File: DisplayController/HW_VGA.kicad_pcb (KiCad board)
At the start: 2 copper layers, 150 x 90 mm, 77 parts, among them J1 Conn_02x40_Odd_Even, J301 Conn_01x02, J401 Conn_01x06, U102 GAL22V10, U103 74ALS163, U104 74ALS163, U105 74ALS163, U202 GAL22V10, U203 74ALS163, U204 74ALS163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

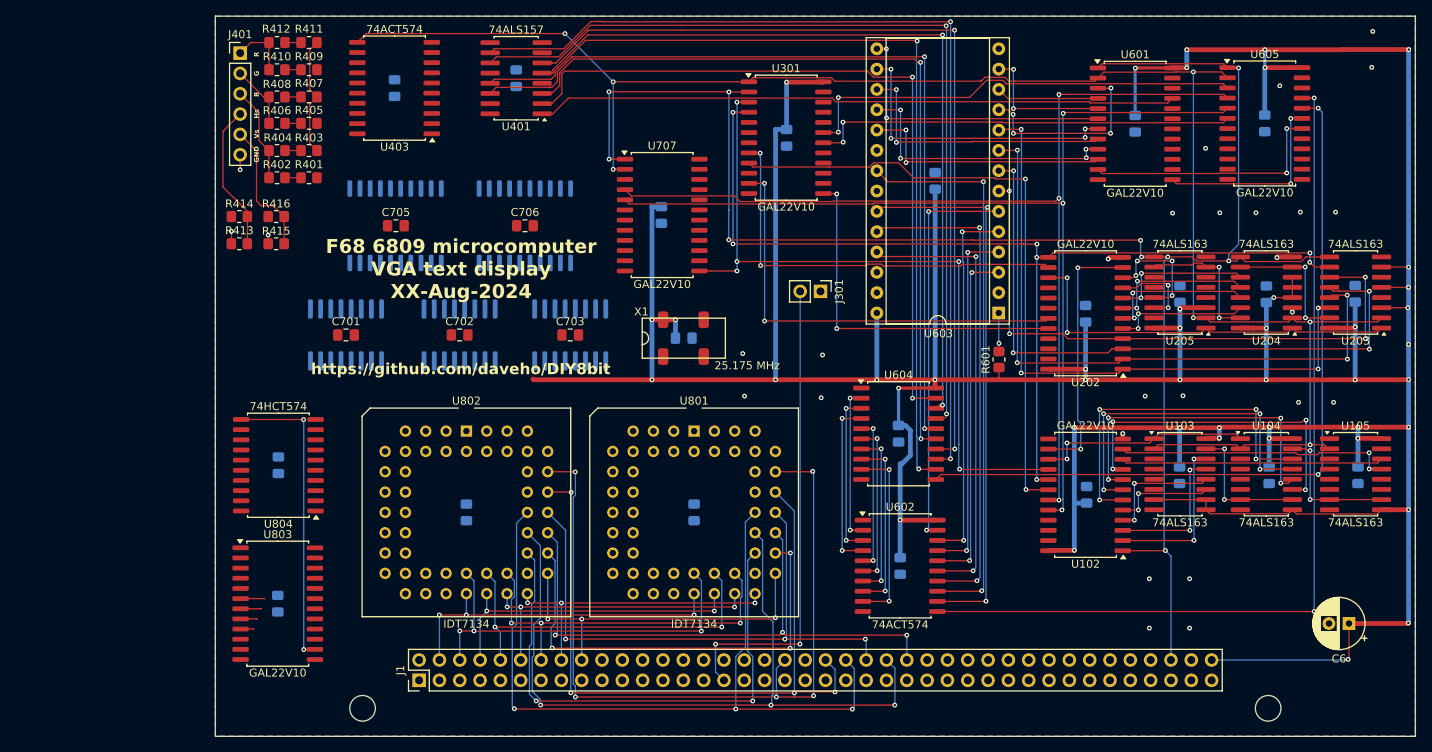
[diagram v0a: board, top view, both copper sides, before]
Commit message: most/all host A/D bus signals are routed
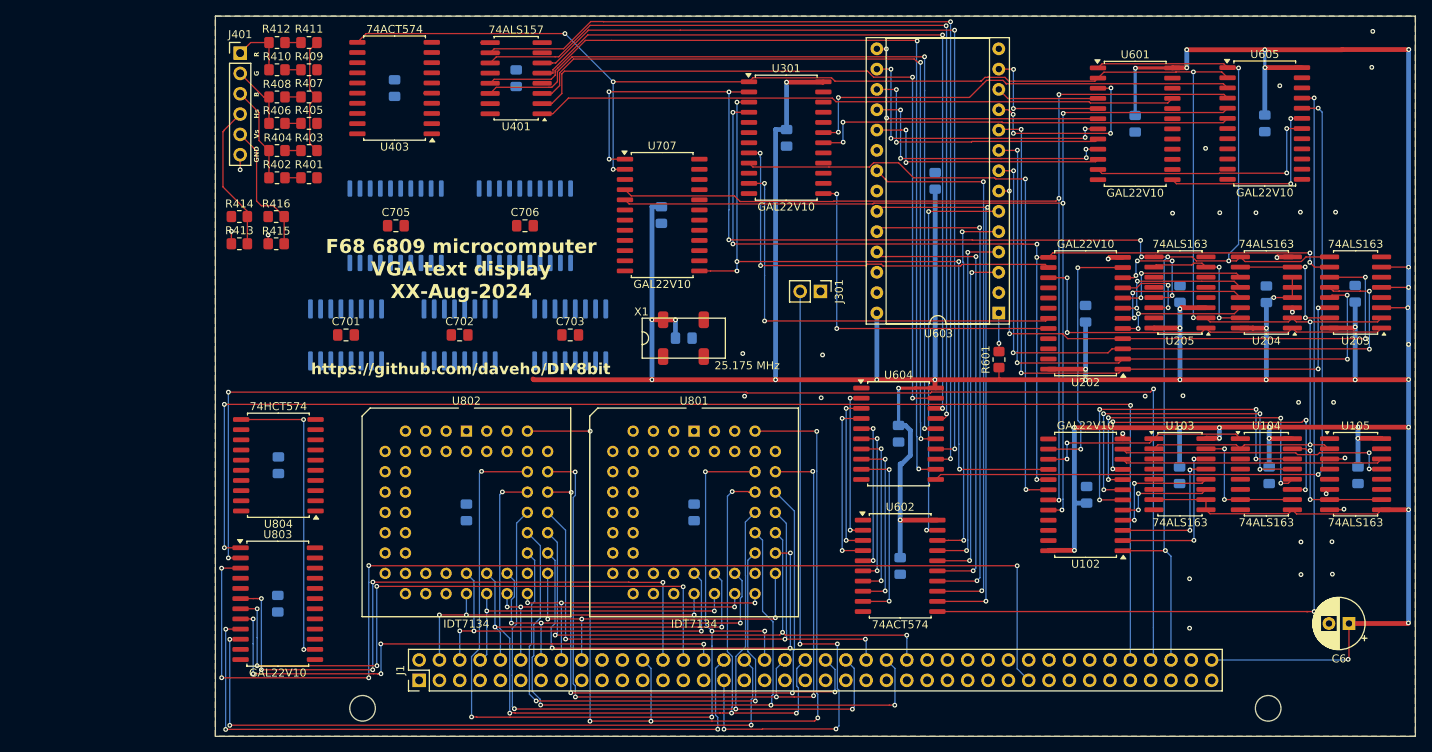
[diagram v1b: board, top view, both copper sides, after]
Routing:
- net /-HostWMEM: track 0.00 -> 172.2 mm, vias 0 -> 3
- net /-HostRMEM: track 0.00 -> 165.1 mm, vias 0 -> 3
- net /~{IODEV7}: track 0.00 -> 144.5 mm, vias 0 -> 5
- net /HostA10: track 0.00 -> 124.5 mm, vias 0 -> 5
- net /HostA0: track 0.00 -> 114.5 mm, vias 0 -> 6
- net /HostA2: track 0.00 -> 105.7 mm, vias 0 -> 5
- net /HostA15: track 0.00 -> 85.9 mm, vias 0 -> 3
- net /HostA14: track 1.65 -> 85.1 mm, vias 0 -> 3
- net /HostA11: track 3.03 -> 82.4 mm, vias 0 -> 5
- net /HostA12: track 2.61 -> 81.6 mm, vias 0 -> 5
- net /HostA13: track 2.08 -> 70.7 mm, vias 0 -> 5
- net /IRQ6: track 59.6 -> 79.8 mm, vias 2 -> 4
- net GND: track 6.96 -> 11.5 mm, vias 26 -> 31

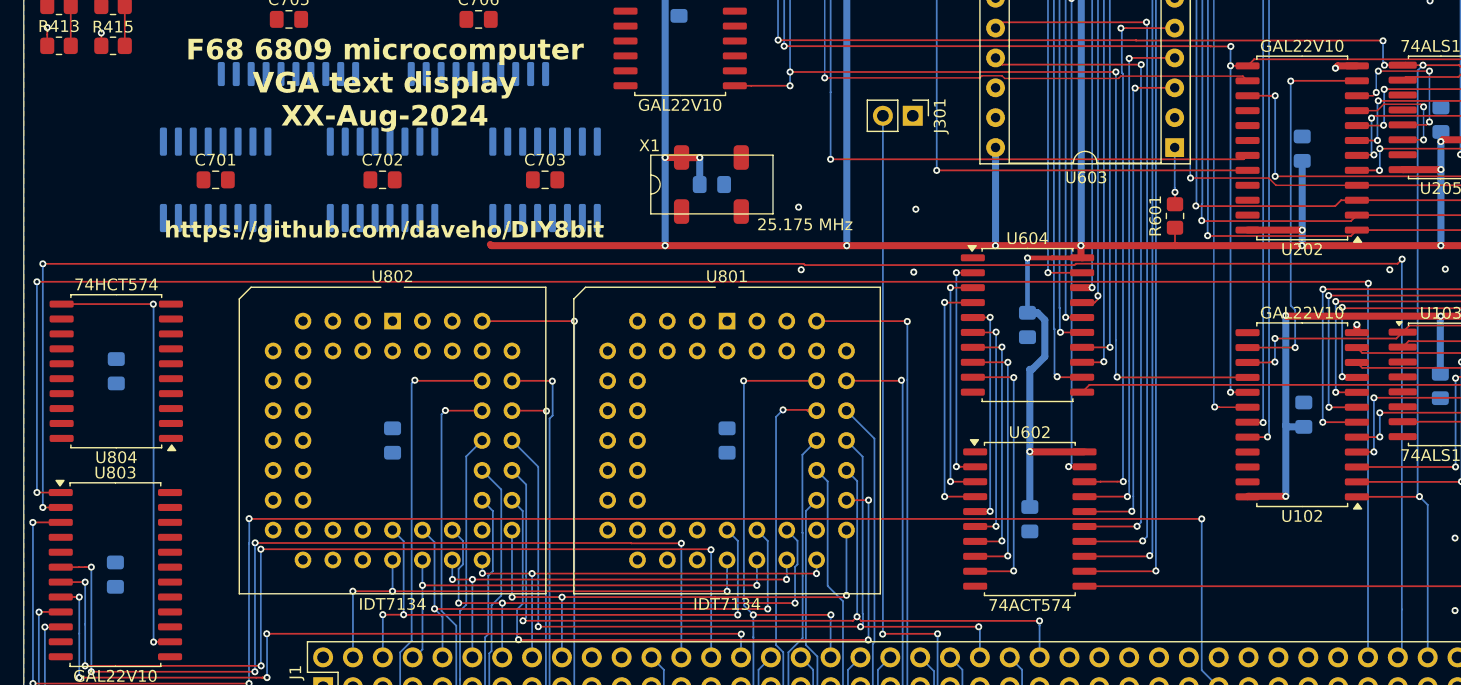
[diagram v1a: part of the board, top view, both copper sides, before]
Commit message: routed some VCC connections
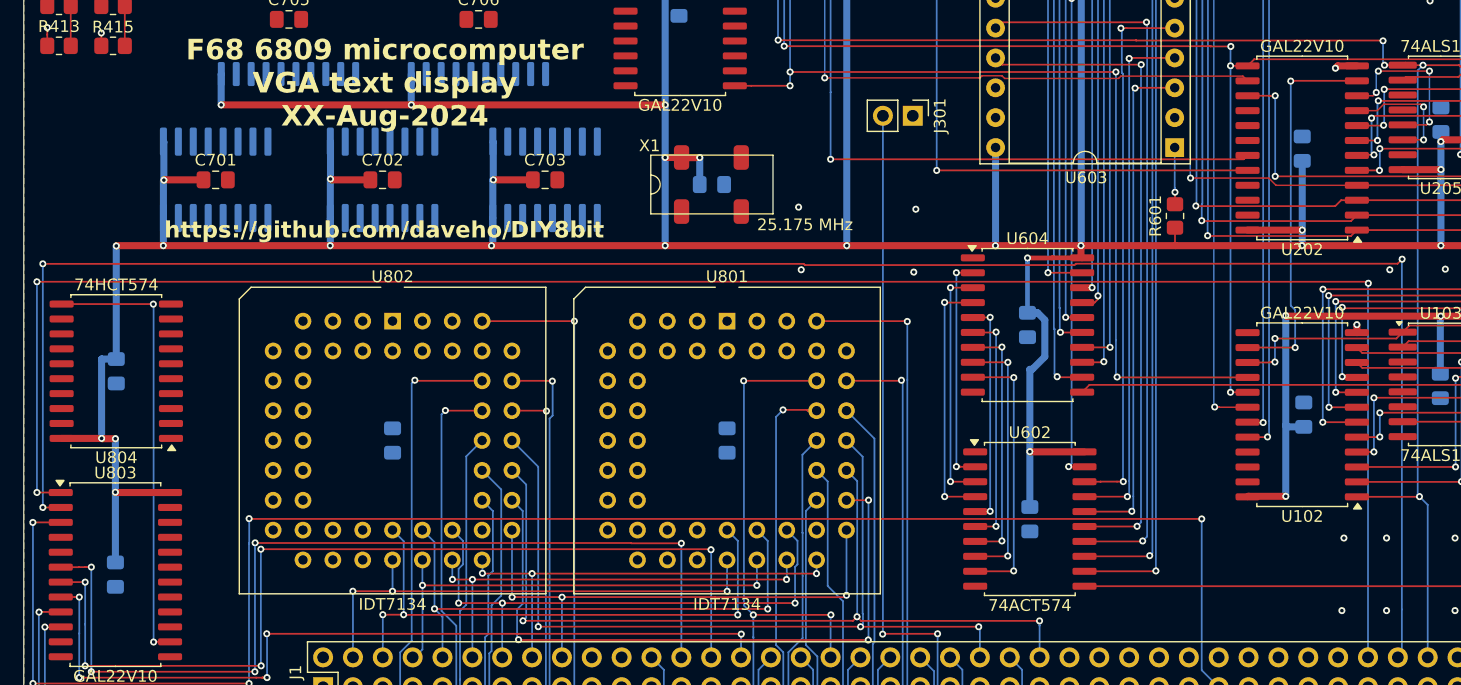
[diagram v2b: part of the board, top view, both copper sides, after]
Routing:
- net VCC: track 593.9 -> 743.0 mm, vias 43 -> 56
- net GND: vias 31 -> 35

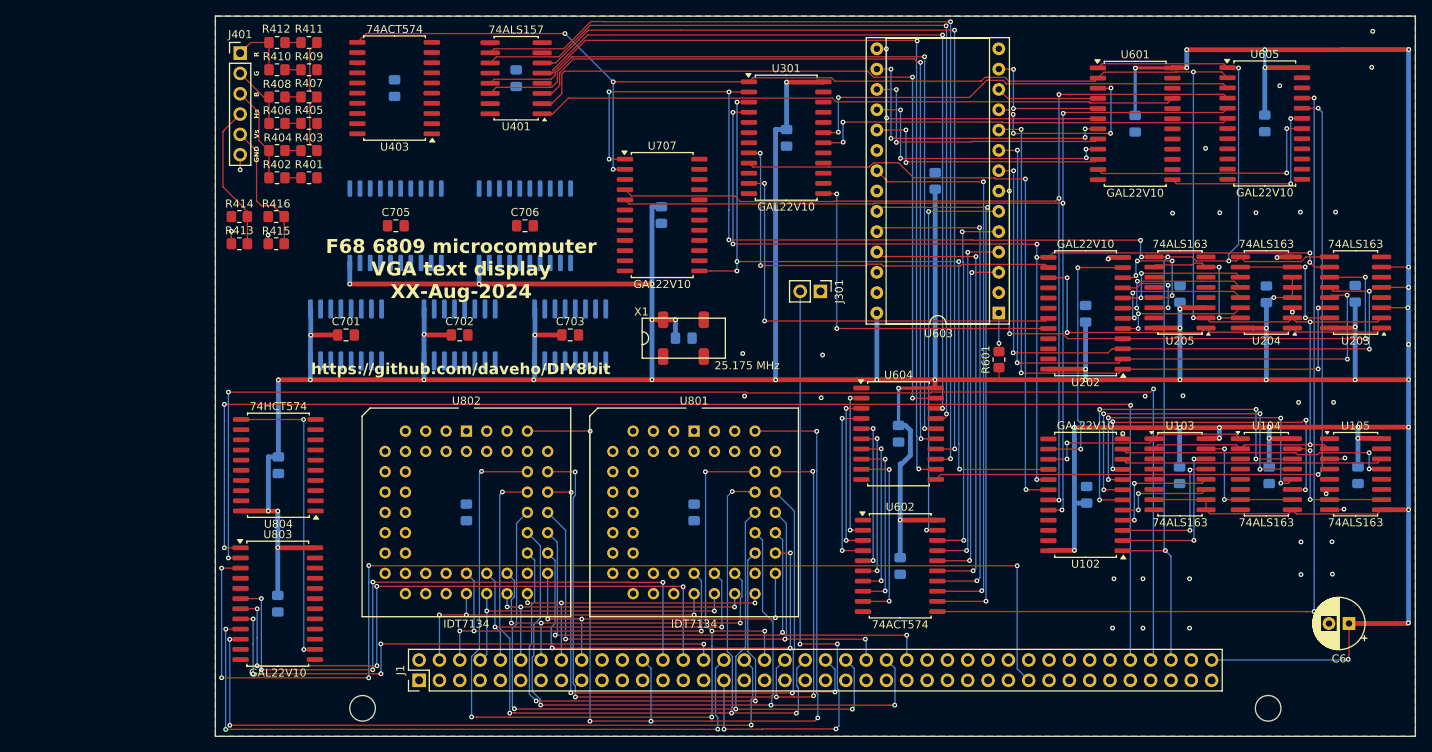
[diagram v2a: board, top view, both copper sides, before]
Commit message: getting close...mostly just the VRAM now
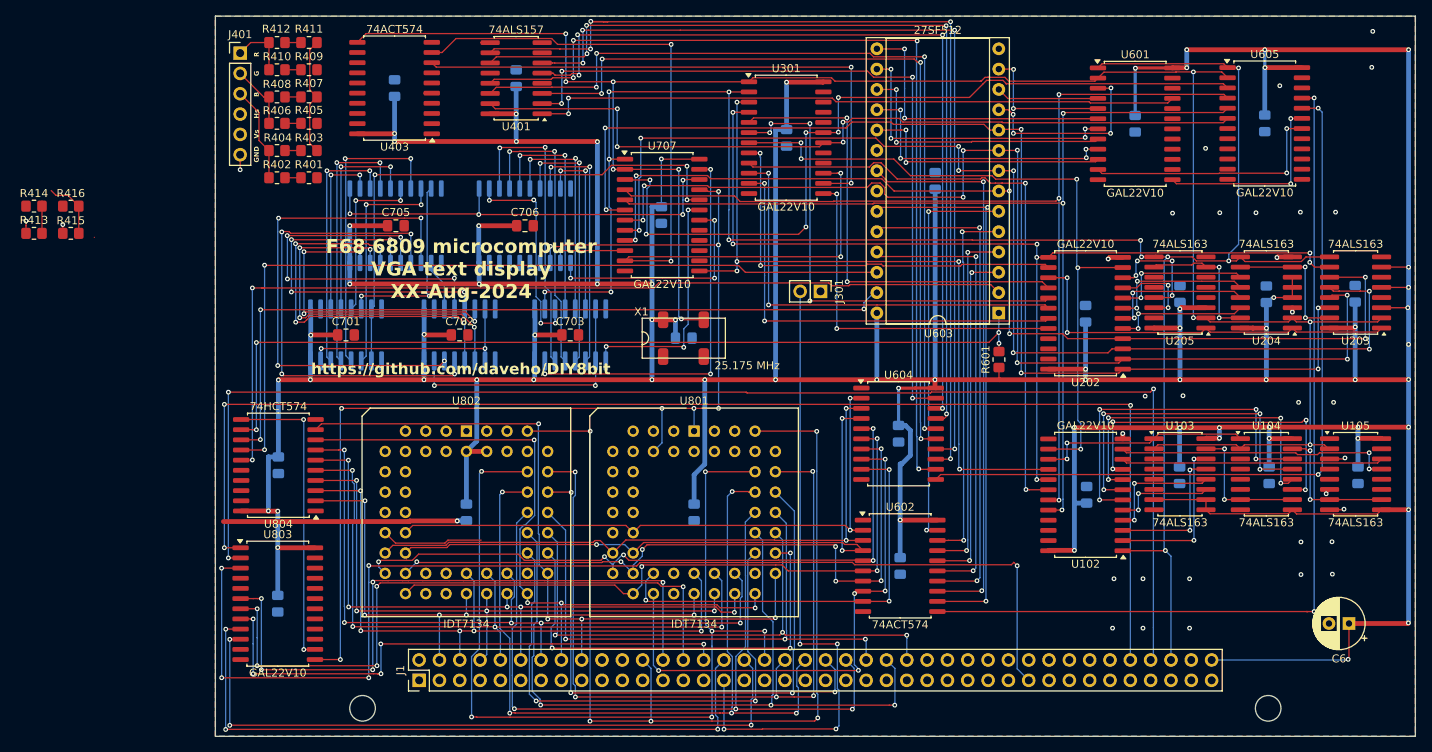
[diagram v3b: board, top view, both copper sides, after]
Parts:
- moved R414 25.7 mm to (40.8, 82.1)
- moved R413 25.7 mm to (40.8, 85.5)
- moved R416 25.7 mm to (45.4, 82.1)
- moved R415 25.7 mm to (45.4, 85.5)
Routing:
- net /ReadoutA12: track 0.00 -> 143.2 mm, vias 0 -> 8
- net VCC: track 743.0 -> 870.8 mm, vias 56 -> 67
- net /FontA12: track 0.00 -> 117.3 mm, vias 0 -> 2
- net /FontA15: track 4.84 -> 111.0 mm, vias 1 -> 4
- net /VSync: track 0.00 -> 103.6 mm, vias 0 -> 4
- net /FontA13: track 0.00 -> 102.9 mm, vias 0 -> 2
- net /FontA14: track 0.00 -> 97.0 mm, vias 0 -> 3
- net /HSync: track 0.00 -> 70.7 mm, vias 0 -> 2
- net /Readout/IncrReadoutAddr: track 0.00 -> 68.7 mm, vias 0 -> 3
- net /ReadoutD3: track 19.3 -> 85.9 mm, vias 2 -> 5
- net /ReadoutD5: track 21.3 -> 86.7 mm, vias 2 -> 7
- net /ReadoutA4: track 0.00 -> 63.0 mm, vias 0 -> 4
- net /VC0: track 79.7 -> 142.3 mm, vias 4 -> 6
- net /VC2: track 81.8 -> 143.5 mm, vias 4 -> 8
- net /ReadoutD4: track 20.3 -> 81.5 mm, vias 2 -> 3
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
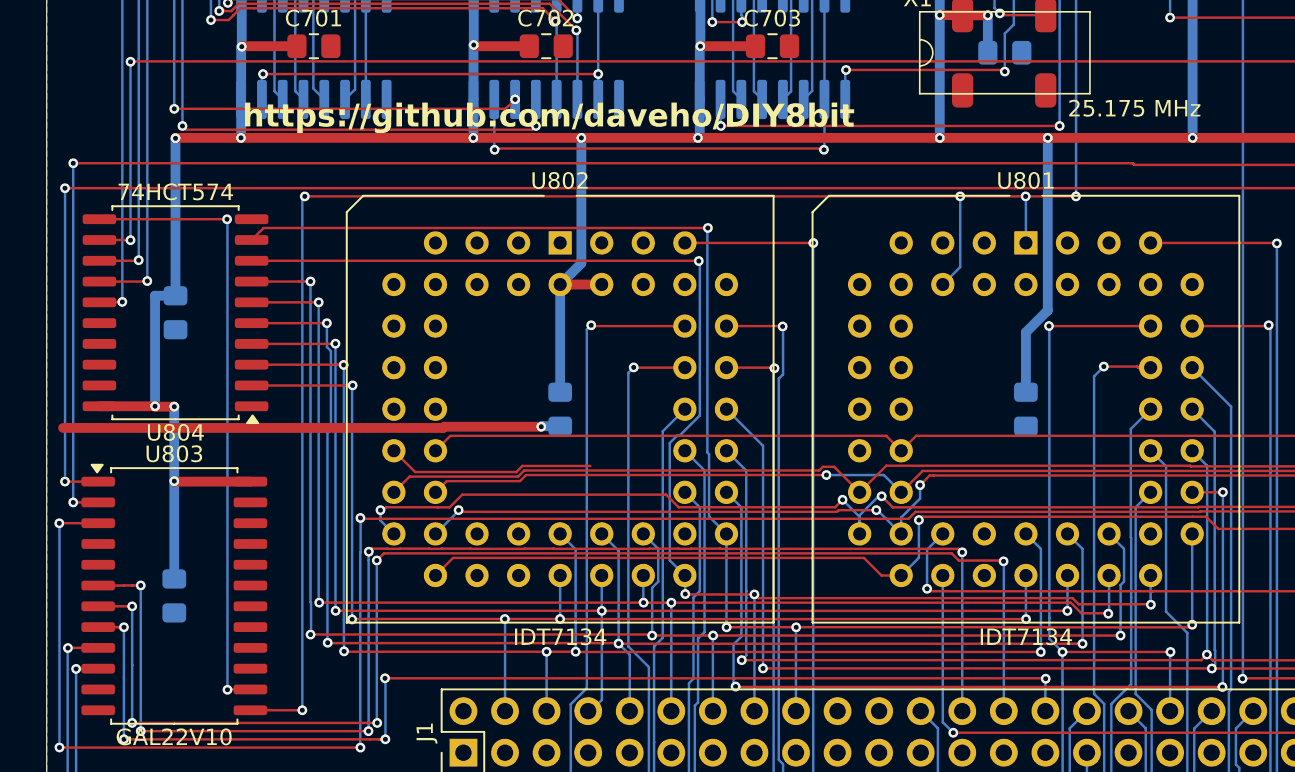
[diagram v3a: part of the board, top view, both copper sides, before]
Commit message: more VRAM trace routing
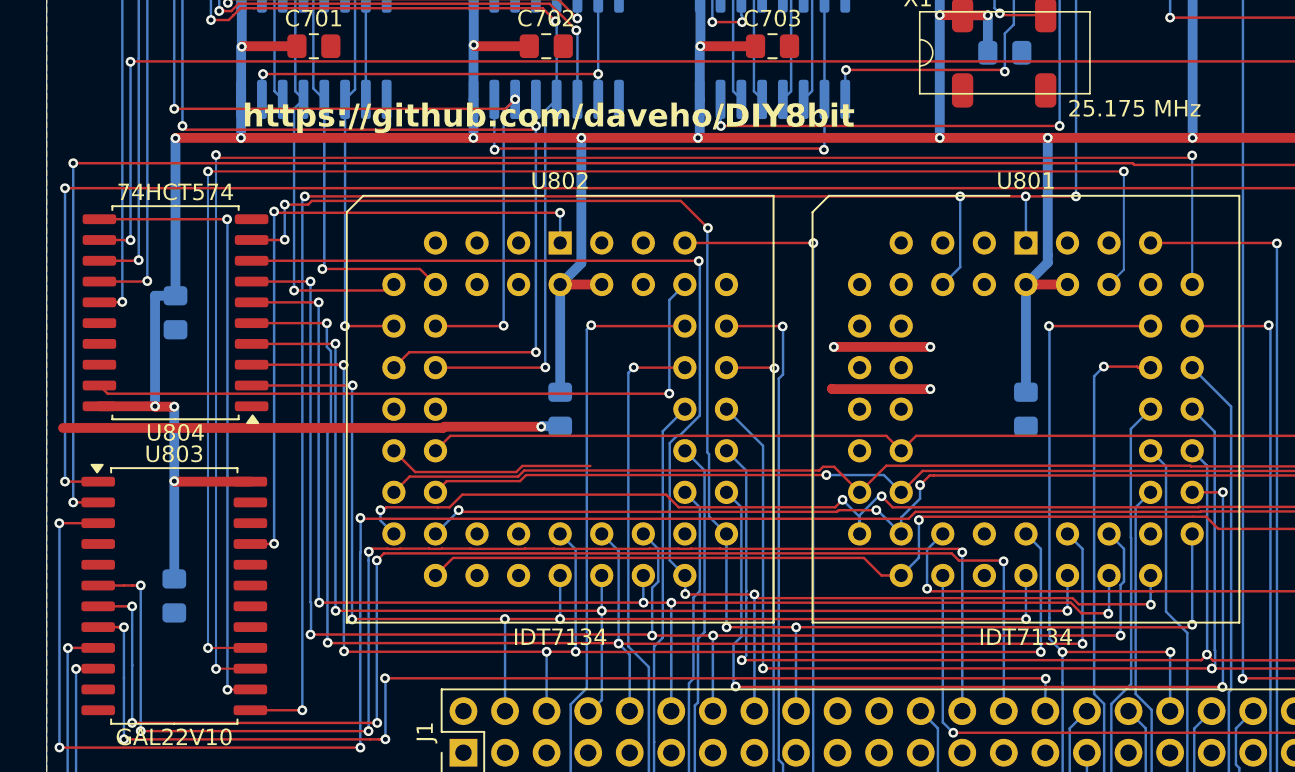
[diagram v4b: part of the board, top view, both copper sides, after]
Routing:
- net /VRAM/-LowerOE: track 0.00 -> 101.2 mm, vias 0 -> 3
- net /VRAM/LowerR/-W: track 0.00 -> 95.0 mm, vias 0 -> 3
- net /VRAM/BankA11: track 0.00 -> 42.1 mm, vias 0 -> 1
- net /VRAM/-ReadoutA12: track 0.00 -> 41.1 mm, vias 0 -> 3
- net /ReadoutA5: track 61.1 -> 85.6 mm, vias 4 -> 5
- net /ReadoutA6: track 49.1 -> 72.5 mm, vias 4 -> 5
- net /ReadoutA4: track 63.0 -> 81.3 mm, vias 4 -> 5
- net /ReadoutA1: track 33.6 -> 51.8 mm, vias 2 -> 3
- net /ReadoutA2: track 37.6 -> 55.3 mm, vias 2 -> 3
- net /ReadoutA3: track 28.7 -> 45.6 mm, vias 2 -> 3
- net GND: track 41.9 -> 53.8 mm, vias 32 -> 35
- net /HostD7: track 92.3 -> 95.1 mm, vias 4 -> 6
- net VCC: track 870.8 -> 873.3 mm

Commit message: routed all VRAM signals!
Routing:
- net /VRAM/-LowerCE: track 0.00 -> 82.0 mm, vias 0 -> 3
- net /ReadoutA7: track 46.4 -> 95.1 mm, vias 4 -> 5
- net /VRAM/-UpperCE: track 0.00 -> 48.3 mm, vias 0 -> 2
- net /ReadoutA8: track 38.0 -> 86.1 mm, vias 2 -> 3
- net /VRAM/-UpperOE: track 0.00 -> 47.5 mm, vias 0 -> 2
- net /ReadoutA5: track 85.6 -> 130.4 mm, vias 5 -> 7
- net /VRAM/UpperR/-W: track 0.00 -> 42.9 mm, vias 0 -> 3
- net /ReadoutA11: track 32.1 -> 71.7 mm, vias 2 -> 3
- net /ReadoutA9: track 49.7 -> 88.9 mm, vias 2 -> 3
- net /ReadoutA10: track 33.1 -> 70.6 mm, vias 2 -> 3
- net /ReadoutA6: track 72.5 -> 103.6 mm, vias 5 -> 6
- net /ReadoutA4: track 81.3 -> 107.3 mm
- net /VRefresh: track 0.00 -> 23.5 mm, vias 0 -> 1
- net /Readout/-LoadReadoutAddr: track 30.4 -> 46.0 mm, vias 3 -> 4
- net /VRAM/-ReadoutA12: track 41.1 -> 45.9 mm, vias 3 -> 4
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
